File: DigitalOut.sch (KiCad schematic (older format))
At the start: 1 part, among them IC3 NCV8402ASTT1G

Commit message: Checkpoint before trying 4 layer
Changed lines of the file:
@@
 $Descr A4 11693 8268
 encoding utf-8
-Sheet 11 50
+Sheet 22 37
 Title ""
 Date ""
@@
 AR Path="/60DB3737/60450D7B" Ref="IC15"  Part="1"
 AR Path="/60DB6C41/60450D7B" Ref="IC16"  Part="1"
-F 0 "IC3" H 5650 3815 50  0000 C CNN
+AR Path="/61F2054A/60450D7B" Ref="IC27"  Part="1"
+AR Path="/6244D324/60450D7B" Ref="IC1"  Part="1"
+F 0 "IC14" H 5650 3815 50  0000 C CNN
 F 1 "NCV8402ASTT1G" H 5650 3724 50  0000 C CNN
 F 2 "SamacSys_Parts:SOT230P700X175-4N" H 6000 3650 50  0001 L CNN

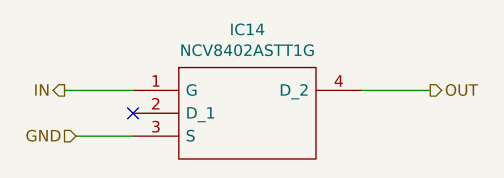
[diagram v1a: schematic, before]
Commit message: 4 layer board that passes checks
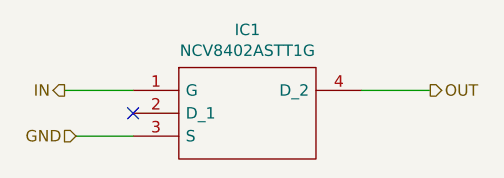
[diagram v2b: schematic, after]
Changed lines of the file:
@@
 $Descr A4 11693 8268
 encoding utf-8
-Sheet 22 37
+Sheet 10 36
 Title ""
 Date ""
@@
 AR Path="/61F2054A/60450D7B" Ref="IC27"  Part="1"
 AR Path="/6244D324/60450D7B" Ref="IC1"  Part="1"
-F 0 "IC14" H 5650 3815 50  0000 C CNN
+F 0 "IC1" H 5650 3815 50  0000 C CNN
 F 1 "NCV8402ASTT1G" H 5650 3724 50  0000 C CNN
 F 2 "SamacSys_Parts:SOT230P700X175-4N" H 6000 3650 50  0001 L CNN

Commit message: Routed PCB
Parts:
- IC3: JLCPCB_PN (none) -> C77755
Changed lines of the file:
@@
 F 8 "ON Semiconductor" H 6000 3050 50  0001 L CNN "Manufacturer_Name"
 F 9 "NCV8402ASTT1G" H 6000 2950 50  0001 L CNN "Manufacturer_Part_Number"
+F 10 "C77755" H 5150 3550 50  0001 C CNN "JLCPCB_PN"
 	1    5150 3550
 	1    0    0    -1
